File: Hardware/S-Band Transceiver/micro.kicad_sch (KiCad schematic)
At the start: 46 parts, among them J3 AVR-UPDI-6, J4 USB_C_Receptacle_USB2.0_16P, SW1 SW_Push, U2 AVR128DA48x-xPT, U3 ADS1118IDGS, U4 FT231XQ

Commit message: Updates to schematic
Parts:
- U3: Digikey (none) -> 296-38850-1-ND
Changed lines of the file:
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@@
+			)
+		)
+		(property "Digikey" "296-38850-1-ND"
+			(at 120.65 158.75 0)
+			(effects
+				(font
+					(size 1.27 1.27)
+				)
+				(hide yes)
 			)
 		)

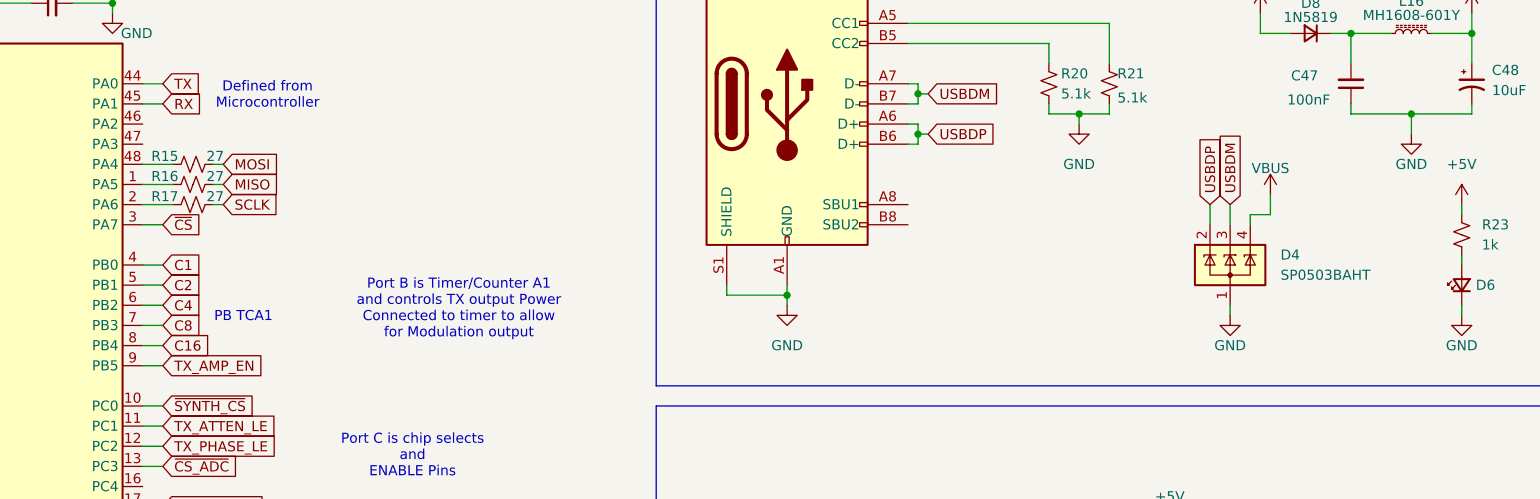
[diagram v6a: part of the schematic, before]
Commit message: Updating notes in schematic
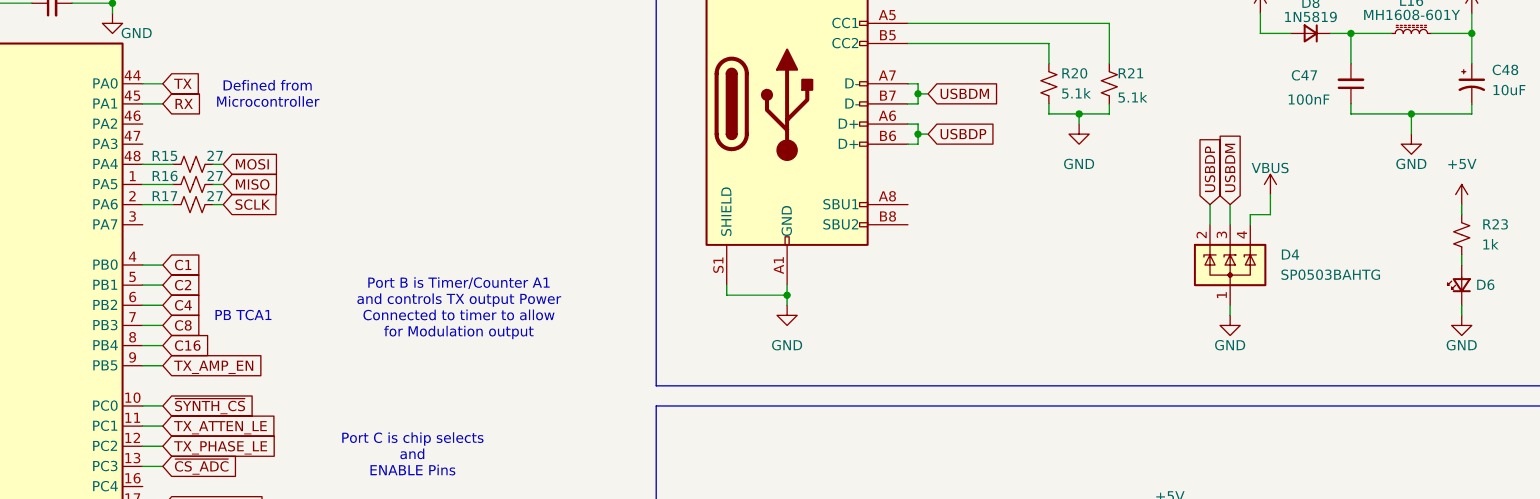
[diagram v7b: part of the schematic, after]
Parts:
- D4: value SP0503BAHT -> SP0503BAHTG; Digikey (none) -> F2715CT-ND
- J4: Digikey (none) -> 2073-USB4085-GF-ACT-ND
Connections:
- net ~{CS}: no longer names the net of U2.3 (PA7)
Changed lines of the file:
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@@
-	(wire
-		(pts
-			(xy 100.33 55.88) (xy 102.87 55.88)
-		)
-		(stroke
-			(width 0)
-			(type default)
-		)
-	)
 	(wire
 		(pts
@@
 		(property "Intersheetrefs" "${INTERSHEET_REFS}"
 			(at 108.0323 38.1 0)
-			(effects
-				(font
-					(size 1.27 1.27)
-				)
-				(justify left)
-				(hide yes)
-			)
-		)
-	)
-	(global_label "~{CS}"
-		(shape input)
-		(at 102.87 55.88 0)
-		(fields_autoplaced yes)
-		(effects
-			(font
-				(size 1.27 1.27)
-			)
-			(justify left)
-		)
-		(property "Intersheetrefs" "${INTERSHEET_REFS}"
-			(at 108.3347 55.88 0)
 			(effects
 				(font
@@
 			)
 		)
-		(property "Value" "SP0503BAHT"
+		(property "Value" "SP0503BAHTG"
 			(at 243.84 62.2299 0)
 			(effects
@@
 		)
 		(property "Description" "TVS Diode Array, 5.5V Standoff, 3 Channels, SOT-143 package"
+			(at 237.49 60.96 0)
+			(effects
+				(font
+					(size 1.27 1.27)
+				)
+				(hide yes)
+			)
+		)
+		(property "Digikey" "F2715CT-ND"
 			(at 237.49 60.96 0)
 			(effects
@@
 			(at 181.61 40.64 0)
 			(effects
+				(font
+					(size 1.27 1.27)
+				)
+				(hide yes)
+			)
+		)
+		(property "Digikey" "2073-USB4085-GF-ACT-ND"
+			(at 181.61 40.64 0)
+			(effects

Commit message: updating values
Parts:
- C39, C40: value 10nF -> 100nF
- R13, R14: value 1k -> 10k
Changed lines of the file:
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@@
 		(dnp no)
 		(property "Reference" "R14"
-			(at 90.678 158.242 90)
+			(at 91.948 157.988 90)
 			(effects
 				(font
@@
 			)
 		)
-		(property "Value" "1k"
+		(property "Value" "10k"
 			(at 87.376 157.988 90)
 			(effects
@@
 			)
 		)
-		(property "Value" "1k"
+		(property "Value" "10k"
 			(at 86.614 151.638 90)
 			(effects
@@
 			)
 		)
-		(property "Value" "10nF"
+		(property "Value" "100nF"
 			(at 103.632 162.306 0)
 			(effects
@@
 			)
 		)
-		(property "Value" "10nF"
+		(property "Value" "100nF"
 			(at 96.012 162.306 0)
 			(effects
